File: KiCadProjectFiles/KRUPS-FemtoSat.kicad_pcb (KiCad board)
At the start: 4 copper layers, 29.2 x 66 mm, 48 parts, among them J1 XT30U Male Connector, J2 54-00170, J3 USB_C_Receptacle_USB2.0_16P, Q1 IRF7410, Q2 IRF7410, SW1 Enable Switch, SW2 Enclosure Detector, SW3 Enclosure Detector, U1 BME280, U2 ESP32-S3-WROOM-1U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

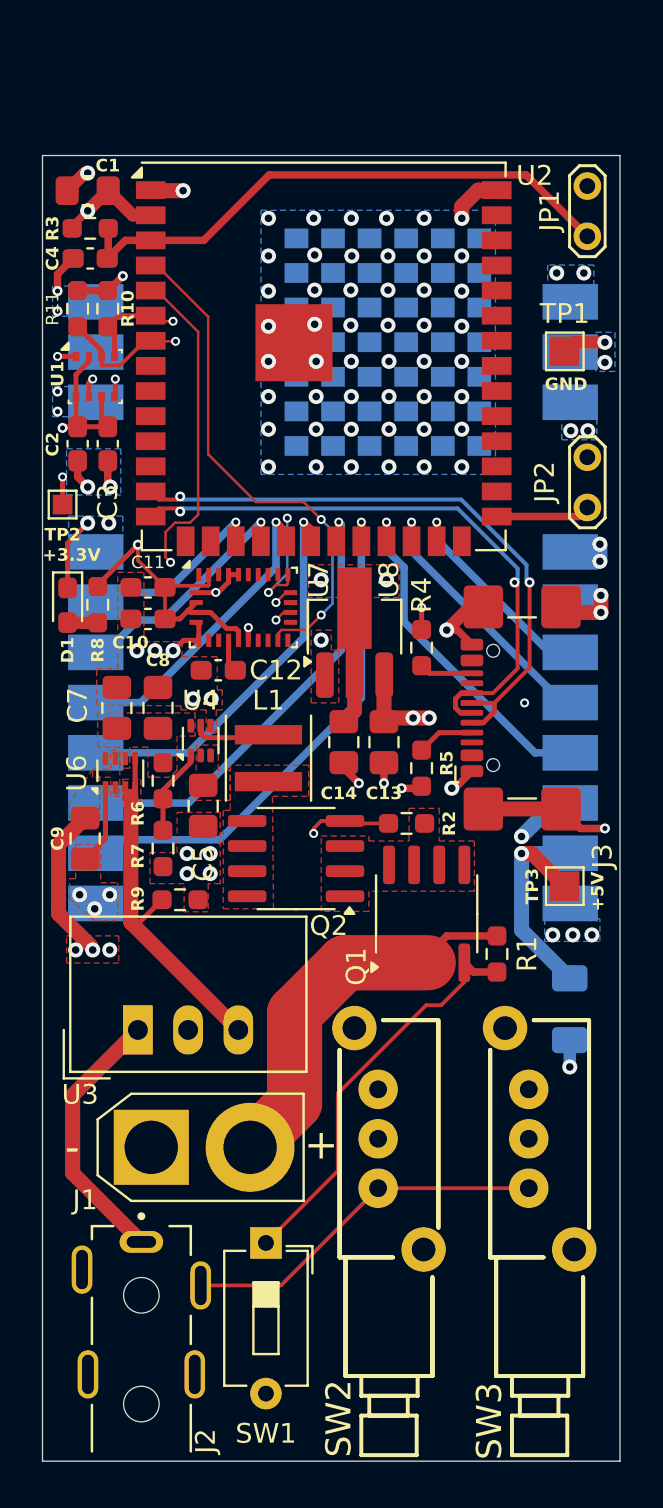
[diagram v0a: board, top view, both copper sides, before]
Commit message: V1.1 Update
- Replaced the ESP32-S3-WROOM-1U module with an ESP32-S3-WROOM-2 module (octal SPI flash, integrated PCB antenna)
- Changed the pins assigned to LORA_TXEN/RXEN to avoid possible issues with 1.8V logic levels on IO47 & IO48
- Updated relevant documentation
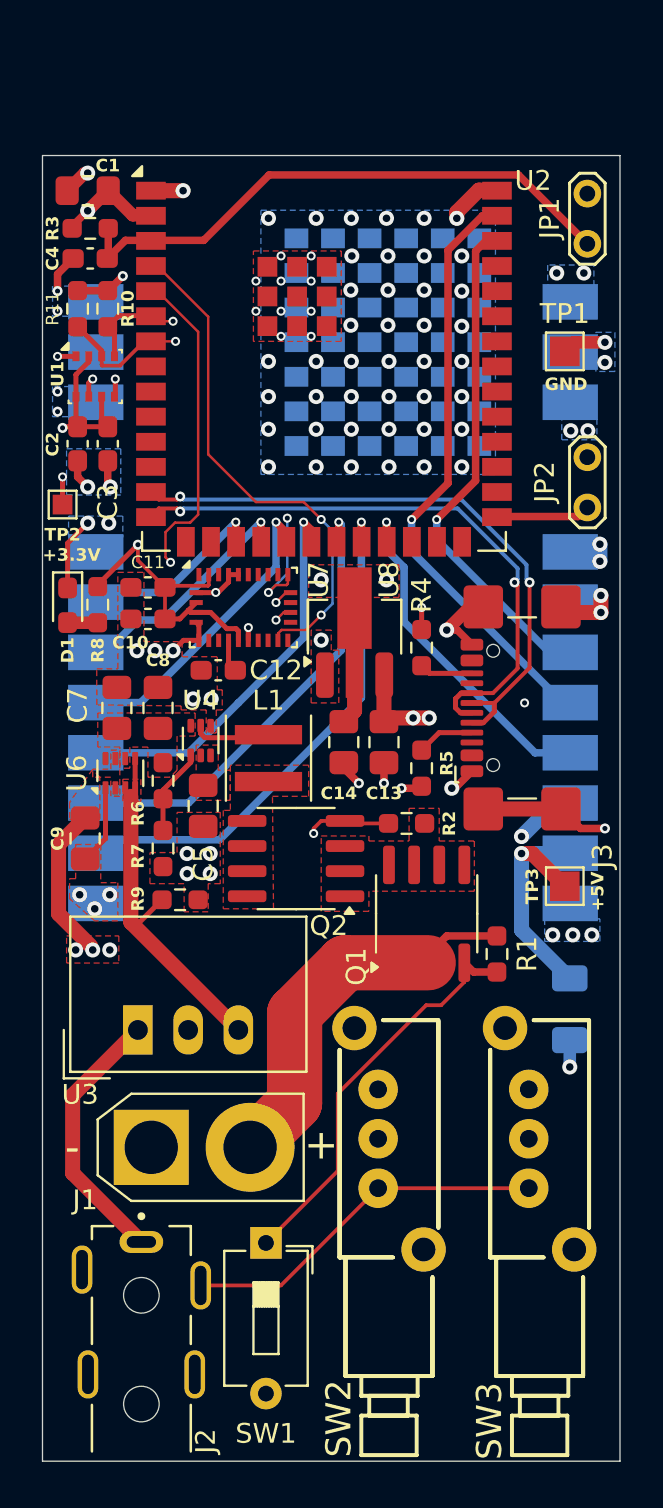
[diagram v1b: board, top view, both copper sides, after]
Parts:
- U2: value ESP32-S3-WROOM-1U -> ESP32-S3-WROOM-2; footprint RF_Module:ESP32-S3-WROOM-1U -> RF_Module:ESP32-S3-WROOM-2
- moved U2 3.12 mm to (103.1, 35.0)
- moved JP1 0.38 mm to (116.5, 29.9)
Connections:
- U2 pad 24: /LORA_TXEN -> unconnected-(U2-IO47-Pad24)
- U2 pad 25: /LORA_RXEN -> unconnected-(U2-IO48-Pad25)
- U2 pad 38: unconnected-(U2-IO2-Pad38) -> /LORA_RXEN
- U2 pad 39: unconnected-(U2-IO1-Pad39) -> /LORA_TXEN
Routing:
- net /LORA_TXEN: track 13.6 -> 30.4 mm
- net /LORA_RXEN: track 11.0 -> 25.8 mm
- net GND: track 59.5 -> 59.6 mm, vias 98 -> 102
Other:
- board text added: "PCB Antenna"

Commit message: changed version marker on back silkscreen to v1.1
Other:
- board text added: "UNIVERSITY OF KENTUCKY KRUPS-FEMTOSAT V1.1 | 10-28-2024 SERIAL NUMBER:"
- board text removed: "UNIVERSITY OF KENTUCKY KRUPS-FEMTOSAT V1 | 10-28-2024 SERIAL NUMBER:"
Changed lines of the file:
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@@
 		(layer "Edge.Cuts")
 	)
-	(gr_text "UNIVERSITY OF KENTUCKY\nKRUPS-FEMTOSAT\nV1 | 10-28-2024\nSERIAL NUMBER:"
+	(gr_text "UNIVERSITY OF KENTUCKY\nKRUPS-FEMTOSAT\nV1.1 | 10-28-2024\nSERIAL NUMBER:"
 		(at 117.475 90.805 0)
 		(layer "B.SilkS")

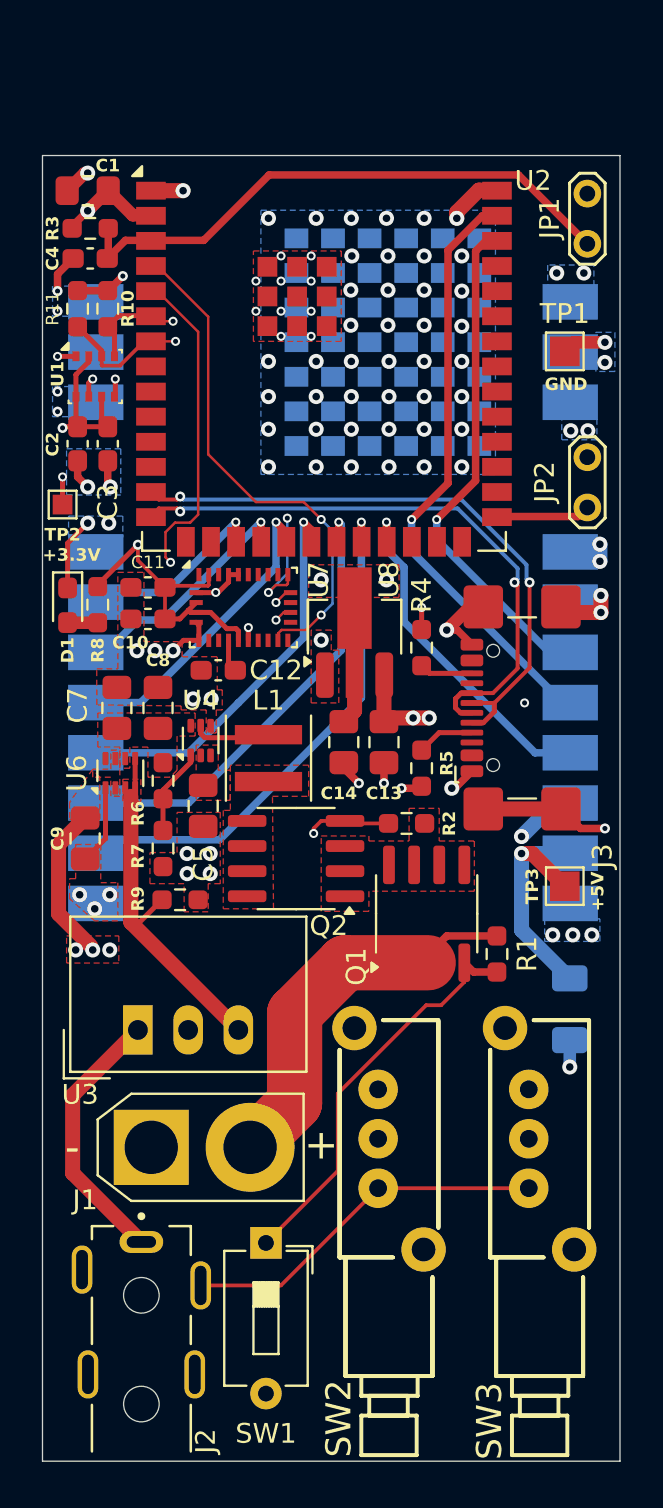
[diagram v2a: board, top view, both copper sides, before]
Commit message: V2 Update. Added mounting holes, moved around some components, and added some silkscreen markers
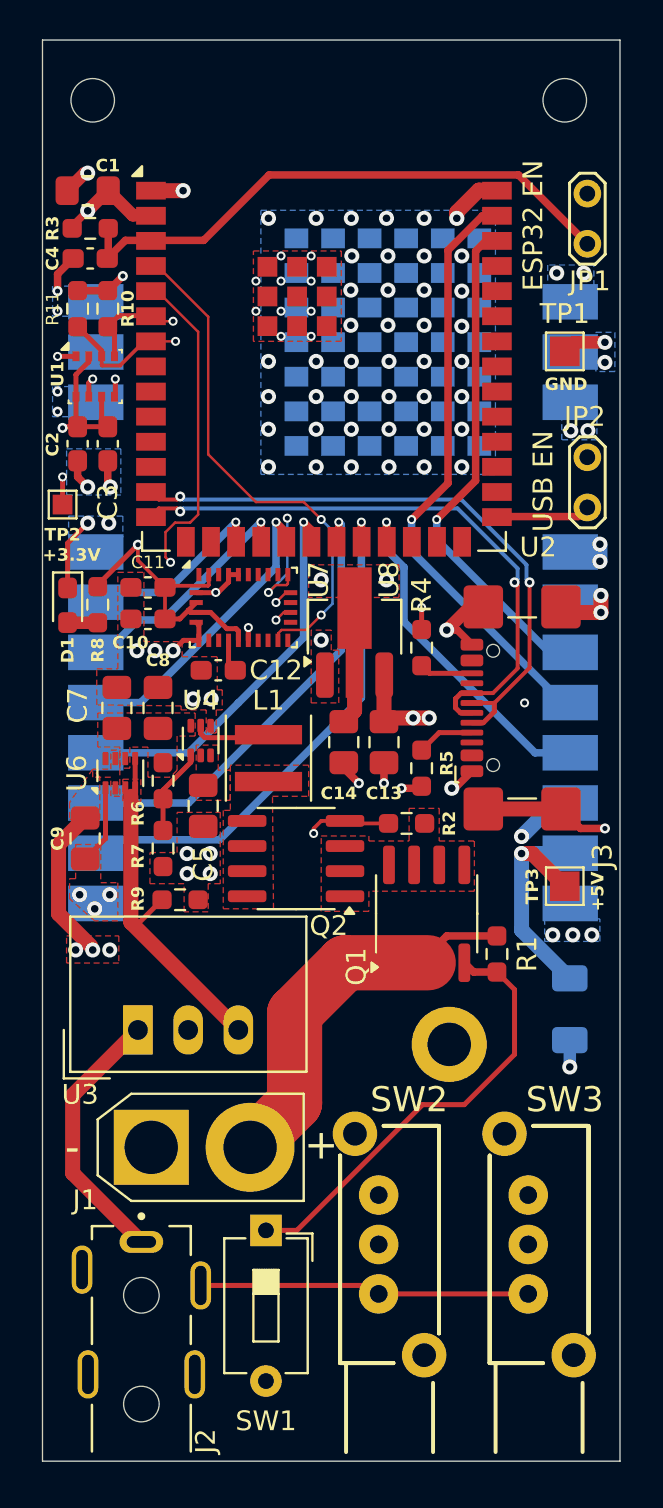
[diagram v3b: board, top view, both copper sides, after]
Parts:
- added H1: MountingHole, MountingHole:MountingHole_2.2mm_M2, F.Cu at (91.4, 25.1)
- added H2: MountingHole, MountingHole:MountingHole_2.2mm_M2, F.Cu at (115.3, 25.1)
- added H3: MountingHole, MountingHole:MountingHole_2.2mm_M2_DIN965_Pad, F.Cu at (109.5, 72.9)
- moved SW2 5.35 mm to (105.9, 80.5)
- moved SW3 5.35 mm to (113.5, 80.5)
- moved SW1 0.64 mm to (100.2, 82.3)
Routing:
- net Net-(SW1-B): track 15.2 -> 9.27 mm
- net Net-(Q2-G): track 24.2 -> 29.6 mm
- net Net-(Q1-G): track 20.6 -> 22.7 mm
- net /PLUG_SWITCH: track 18.6 -> 16.7 mm
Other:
- board size 29.2 x 66 mm -> 29.2 x 71.9 mm
- board text added: "ESP32 EN"
- board text added: "UNIVERSITY OF KENTUCKY KRUPS-FEMTOSAT V2 | 11-10-2024 SERIAL NUMBER:"
- board text added: "USB EN"
- board text removed: "UNIVERSITY OF KENTUCKY KRUPS-FEMTOSAT V1.1 | 10-28-2024 SERIAL NUMBER:"

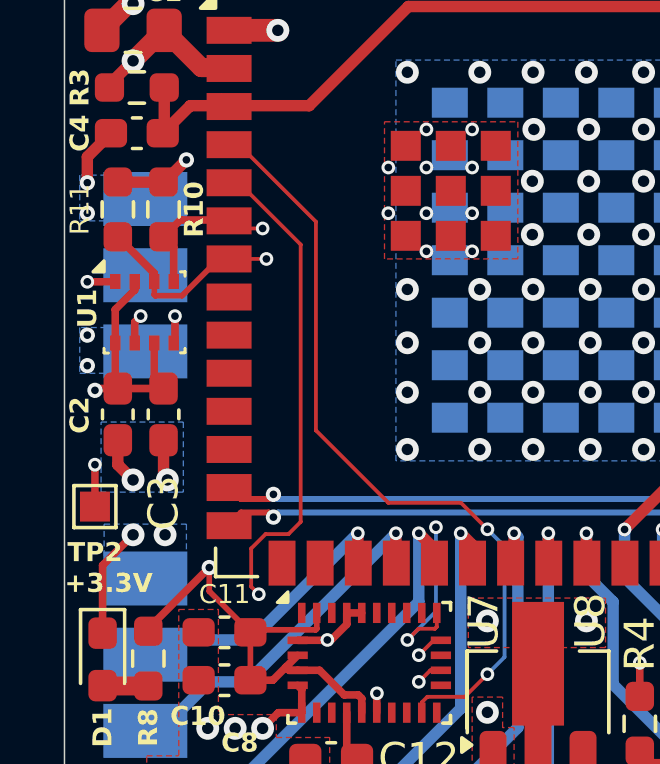
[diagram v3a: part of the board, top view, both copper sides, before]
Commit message: V3. Connected the SPI NSS of the LoRa modem to an IO pin rather than ground
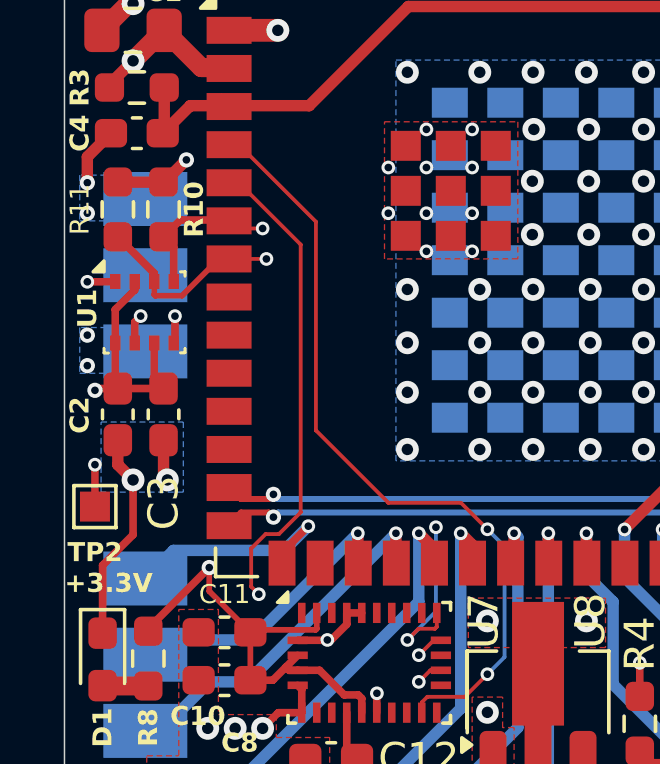
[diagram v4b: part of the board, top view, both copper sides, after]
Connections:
- U2 pad 15: unconnected-(U2-IO3-Pad15) -> /SPI_NSS
- U5 pad 19: GND -> /SPI_NSS
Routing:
- net /SPI_NSS: track 0.00 -> 7.75 mm, vias 0 -> 1
- net GND: track 59.6 -> 61.5 mm, vias 102 -> 100
- net /~{BNO086_RESET}: track 22.4 -> 21.6 mm
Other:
- board text added: "UNIVERSITY OF KENTUCKY KRUPS-FEMTOSAT V3 | 11-11-2024 SERIAL NUMBER:"
- board text removed: "UNIVERSITY OF KENTUCKY KRUPS-FEMTOSAT V2 | 11-10-2024 SERIAL NUMBER:"
